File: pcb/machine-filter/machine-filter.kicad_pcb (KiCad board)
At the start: 2 copper layers, 150 x 107 mm, 156 parts, among them J1 PJ398SM, J10 PJ398SM, J11 PJ398SM, J12 PJ398SM, J13 EURO PWR 2x5, J14 EXPANSION 2x4, J15 TF-01A, J2 PJ398SM, J3 PJ398SM, J4 PJ398SM, J5 PJ398SM, J6 PJ398SM, J7 PJ398SM, J8 PJ398SM, J9 PJ398SM, U1 LMV324, U2 LMV324, U3 TL072, U4 TL072, U5 LM4040-10, U6 74HC4051, U7 LM324, U8 LM324

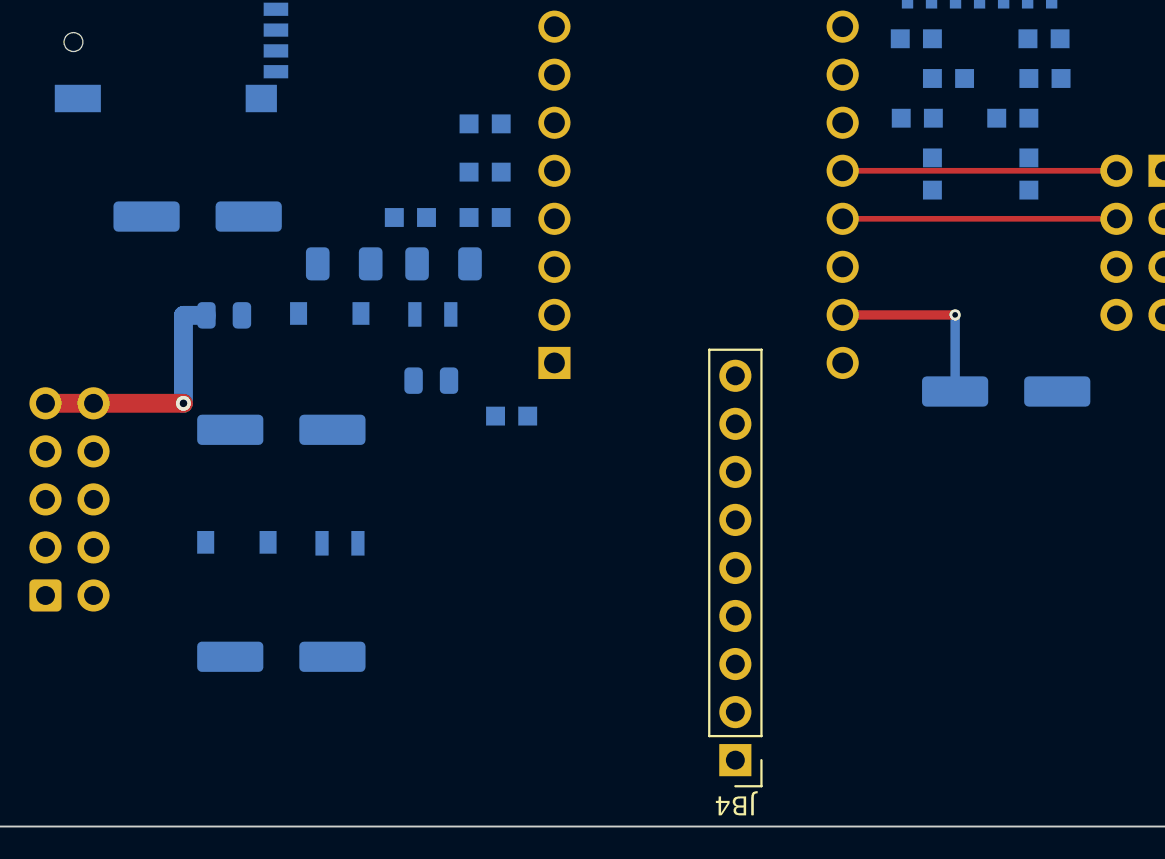
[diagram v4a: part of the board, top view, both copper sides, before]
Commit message: Main board: Seed supply filter (R1, R2, C5) moved to the VIN pin beside C6; FB2 next to J13's -12 V side; microSD pull-ups back in one column
Control board on hold until the main board's zones are done (d).

Co-Authored-By: Claude Opus 5.5 <noreply@anthropic.com>
Claude-Session: https://claude.ai/code/session_01Cf5qNBi3oNHhbCjPHvswth
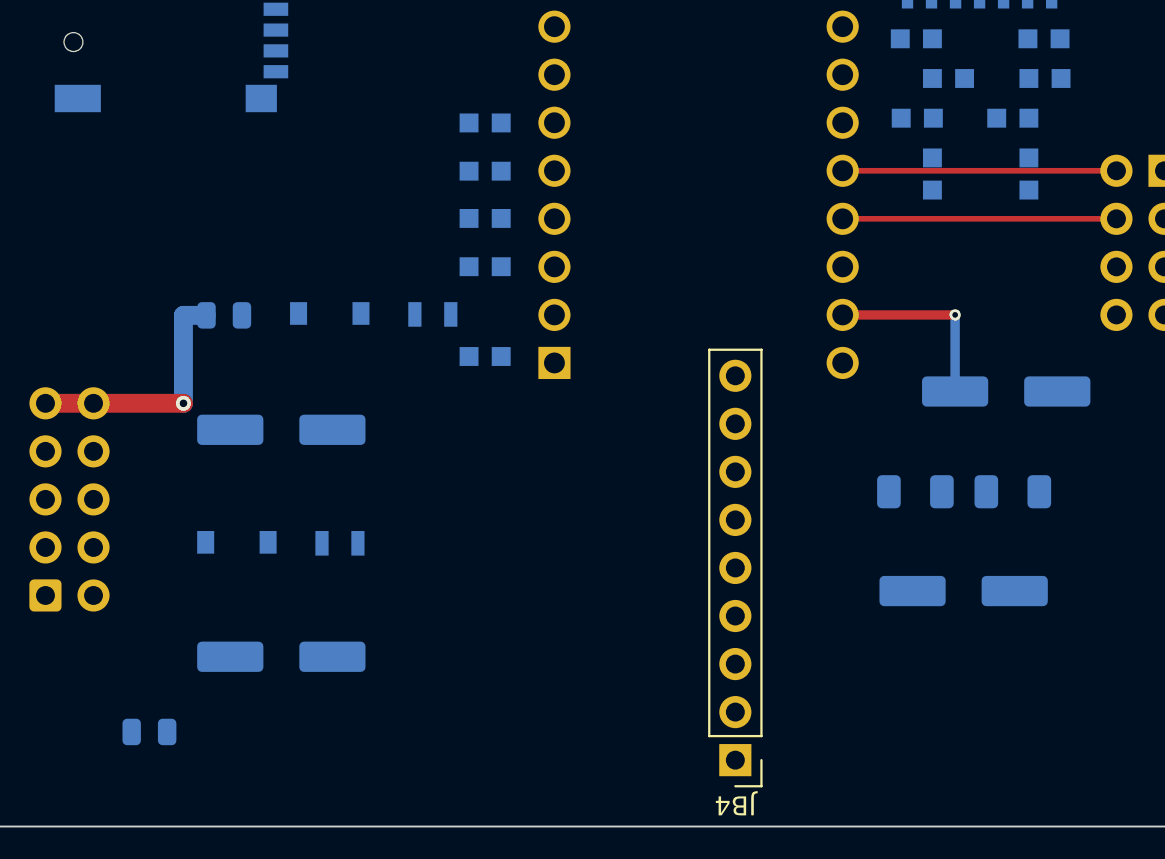
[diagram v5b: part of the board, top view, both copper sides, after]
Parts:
- moved C5 45.1 mm to (235.2, 151.6)
- moved R1 37.3 mm to (237.8, 146.3), turned to 180 degrees
- moved R2 27.7 mm to (232.7, 146.3), turned to 180 degrees
- moved FB2 23.8 mm to (192.2, 159.0)
- moved R100 4.73 mm to (209.9, 134.4)
- moved R101 3.45 mm to (209.9, 139.2)
- moved R103 0.05 mm to (209.9, 129.3)
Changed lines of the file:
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@@
 	(footprint "Capacitor_SMD:CP_Elec_6.3x7.7"
 		(layer "B.Cu")
-		(at 194.75 131.75 180)
+		(at 235.25 151.55 180)
 		(descr "SMD capacitor, aluminum electrolytic, Nichicon, 6.3x7.7mm")
 		(tags "capacitor electrolytic")
@@
 	(footprint "filter-module:R_0603"
 		(layer "B.Cu")
-		(at 209.95 131.8 180)
+		(at 209.95 131.85 180)
 		(descr "Resistor SMD 0603, reflow soldering, Vishay (see dcrcw.pdf)")
 		(tags "resistor 0603")
@@
 	(footprint "filter-module:R_0603"
 		(layer "B.Cu")
-		(at 209.95 126.85 180)
+		(at 209.95 126.8 180)
 		(descr "Resistor SMD 0603, reflow soldering, Vishay (see dcrcw.pdf)")
 		(tags "resistor 0603")
@@
 	(footprint "filter-module:R_1206_3216Metric"
 		(layer "B.Cu")
-		(at 202.5 134.25)
+		(at 237.85 146.3 180)
 		(descr "Resistor SMD 1206 (3216 Metric), square (rectangular) end terminal, IPC_7351 nominal, (Body size source: http://www.tortai-tech.com/upload/download/2011102023233369053.pdf), generated with kicad-footprint-generator")
 		(tags "resistor")
 		(property "Reference" "R1"
-			(at 0 1.82 180)
+			(at 0 1.82 0)
 			(unlocked yes)
 			(layer "B.SilkS")
@@
 		)
 		(property "Value" "3.3 0.75W"
-			(at 0 -1.819999 180)
+			(at 0 -1.819999 0)
 			(unlocked yes)
 			(layer "B.SilkS")
@@
 		)
 		(property "Datasheet" ""
-			(at 0 0 180)
+			(at 0 0 0)
 			(layer "B.Fab")
 			(hide yes)
@@
 		)
 		(property "Description" ""
-			(at 0 0 180)
+			(at 0 0 0)
 			(layer "B.Fab")
 			(hide yes)
@@
 		(duplicate_pad_numbers_are_jumpers no)
 		(fp_line
-			(start -0.602064 -0.91)
-			(end 0.602063 -0.91)
+			(start -0.602064 0.91)
+			(end 0.602063 0.91)
 			(stroke
 				(width 0.12)
@@
 		)
 		(fp_line
-			(start -0.602064 0.91)
-			(end 0.602063 0.91)
+			(start -0.602064 -0.91)
+			(end 0.602063 -0.91)
 			(stroke
 				(width 0.12)
@@
 		)
 		(fp_line
-			(start -2.28 -1.12)
-			(end -2.28 1.12)
+			(start 2.279999 1.12)
+			(end 2.279999 -1.12)
 			(stroke
 				(width 0.05)
@@
 		)
 		(fp_line
-			(start -2.28 1.12)
-			(end 2.279999 1.12)
+			(start 2.279999 -1.12)
+			(end -2.28 -1.12)
 			(stroke
 				(width 0.05)
@@
 		)
 		(fp_line
-			(start 2.279999 -1.12)
-			(end -2.28 -1.12)
+			(start -2.28 1.12)
+			(end 2.279999 1.12)
 			(stroke
 				(width 0.05)
@@
 		)
 		(fp_line
-			(start 2.279999 1.12)
-			(end 2.279999 -1.12)
+			(start -2.28 -1.12)
+			(end -2.28 1.12)
 			(stroke
 				(width 0.05)
@@
 		)
 		(fp_line
-			(start -1.600001 -0.8)
-			(end -1.600001 0.800001)
+			(start 1.6 0.800001)
+			(end 1.6 -0.8)
 			(stroke
 				(width 0.1)
@@
 		)
 		(fp_line
-			(start -1.600001 0.800001)
-			(end 1.6 0.800001)
+			(start 1.6 -0.8)
+			(end -1.600001 -0.8)
 			(stroke
 				(width 0.1)
@@
 		)
 		(fp_line
-			(start 1.6 -0.8)
-			(end -1.600001 -0.8)
+			(start -1.600001 0.800001)
+			(end 1.6 0.800001)
 			(stroke
 				(width 0.1)
@@
 		)
 		(fp_line
-			(start 1.6 0.800001)
-			(end 1.6 -0.8)
+			(start -1.600001 -0.8)
+			(end -1.600001 0.800001)
 			(stroke
 				(width 0.1)
@@
 		)
 		(fp_text user "${REFERENCE}"
-			(at 0 0 180)
+			(at 0 0 0)
 			(unlocked yes)
 			(layer "B.Fab")
@@
 		)
 		(pad "1" smd roundrect
-			(at -1.4 0)
+			(at -1.4 0 180)
 			(size 1.25 1.75)
 			(layers "B.Cu" "B.Mask" "B.Paste")
@@
 		)
 		(pad "2" smd roundrect
-			(at 1.399999 0)
+			(at 1.399999 0 180)
 			(size 1.25 1.75)
 			(layers "B.Cu" "B.Mask" "B.Paste")
@@
 	(footprint "filter-module:R_0603"
 		(layer "B.Cu")
-		(at 209.95 129.4 180)
+		(at 209.95 129.35 180)
 		(descr "Resistor SMD 0603, reflow soldering, Vishay (see dcrcw.pdf)")
 		(tags "resistor 0603")
@@
 	(footprint "filter-module:R_0603"
 		(layer "B.Cu")
-		(at 206 131.8 180)
+		(at 209.95 134.4 180)
 		(descr "Resistor SMD 0603, reflow soldering, Vishay (see dcrcw.pdf)")
 		(tags "resistor 0603")
@@
 	(footprint "filter-module:R_1206_3216Metric"
 		(layer "B.Cu")
-		(at 207.75 134.25)
+		(at 232.7 146.3 180)
 		(descr "Resistor SMD 1206 (3216 Metric), square (rectangular) end terminal, IPC_7351 nominal, (Body size source: http://www.tortai-tech.com/upload/download/2011102023233369053.pdf), generated with kicad-footprint-generator")
 		(tags "resistor")
 		(property "Reference" "R2"
-			(at 0 1.82 180)
+			(at 0 1.82 0)
 			(unlocked yes)
 			(layer "B.SilkS")
@@
 		)
 		(property "Value" "3.3 0.75W"
-			(at 0 -1.82 180)
+			(at 0 -1.82 0)
 			(unlocked yes)
 			(layer "B.SilkS")
@@
 		)
 		(property "Datasheet" ""
-			(at 0 0 180)
+			(at 0 0 0)
 			(layer "B.Fab")
 			(hide yes)
@@
 		)
 		(property "Description" ""
-			(at 0 0 180)
+			(at 0 0 0)
 			(layer "B.Fab")
 			(hide yes)
@@
 		(duplicate_pad_numbers_are_jumpers no)
 		(fp_line
-			(start -0.602064 -0.91)
-			(end 0.602063 -0.91)
+			(start -0.602064 0.91)
+			(end 0.602063 0.91)
 			(stroke
 				(width 0.12)
@@
 		)
 		(fp_line
-			(start -0.602064 0.91)
-			(end 0.602063 0.91)
+			(start -0.602064 -0.91)
+			(end 0.602063 -0.91)
 			(stroke
 				(width 0.12)
@@
 		)
 		(fp_line
-			(start -2.28 -1.12)
-			(end -2.28 1.12)
+			(start 2.279999 1.12)
+			(end 2.279999 -1.12)
 			(stroke
 				(width 0.05)
@@
 		)
 		(fp_line
-			(start -2.28 1.12)
-			(end 2.279999 1.12)
+			(start 2.279999 -1.12)
+			(end -2.28 -1.12)
 			(stroke
 				(width 0.05)
@@
 		)
 		(fp_line
-			(start 2.279999 -1.12)
-			(end -2.28 -1.12)
+			(start -2.28 1.12)
+			(end 2.279999 1.12)
 			(stroke
 				(width 0.05)
@@
 		)
 		(fp_line
-			(start 2.279999 1.12)
-			(end 2.279999 -1.12)
+			(start -2.28 -1.12)
+			(end -2.28 1.12)
 			(stroke
 				(width 0.05)
@@
 		)
 		(fp_line
-			(start -1.600001 -0.8)
-			(end -1.600001 0.8)
+			(start 1.6 0.8)
+			(end 1.6 -0.8)
 			(stroke
 				(width 0.1)
@@
 		)
 		(fp_line
-			(start -1.600001 0.8)
-			(end 1.6 0.8)
+			(start 1.6 -0.8)
+			(end -1.600001 -0.8)
 			(stroke
 				(width 0.1)
@@
 		)
 		(fp_line
-			(start 1.6 -0.8)
-			(end -1.600001 -0.8)
+			(start -1.600001 0.8)
+			(end 1.6 0.8)
 			(stroke
 				(width 0.1)
@@
 		)
 		(fp_line
-			(start 1.6 0.8)
-			(end 1.6 -0.8)
+			(start -1.600001 -0.8)
+			(end -1.600001 0.8)
 			(stroke
 				(width 0.1)
@@
 		)
 		(fp_text user "${REFERENCE}"
-			(at 0 0 180)
+			(at 0 0 0)
 			(unlocked yes)
 			(layer "B.Fab")
@@
 		)
 		(pad "1" smd roundrect
-			(at -1.4 0)
+			(at -1.4 0 180)
 			(size 1.25 1.75)
 			(layers "B.Cu" "B.Mask" "B.Paste")
@@
 		)
 		(pad "2" smd roundrect
-			(at 1.399999 0)
+			(at 1.399999 0 180)
 			(size 1.25 1.75)
 			(layers "B.Cu" "B.Mask" "B.Paste")
@@
 	(footprint "filter-module:R_0805_2012Metric"
 		(layer "B.Cu")
-		(at 207.105 140.425)
+		(at 192.2 159)
 		(descr "Resistor SMD 0805 (2012 Metric), square (rectangular) end terminal, IPC_7351 nominal, (Body size source: https://docs.google.com/spreadsheets/d/1BsfQQcO9C6DZCsRaXUlFlo91Tg2WpOkGARC1WS5S8t0/edit?usp=sharing), generated with kicad-footprint-generator")
 		(tags "resistor")
@@
 	(footprint "filter-module:R_0603"
 		(layer "B.Cu")
-		(at 211.35 142.3 180)
+		(at 209.95 139.15 180)
 		(descr "Resistor SMD 0603, reflow soldering, Vishay (see dcrcw.pdf)")
 		(tags "resistor 0603")
